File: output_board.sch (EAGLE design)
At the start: 27 parts, among them IC1 LTV-846PDIP16, IC2 LTV-846PDIP16, IC3 LTV-846PDIP16, IC4 LTV-846PDIP16

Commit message: Fixed bulk capacitor footprints; made +V for output channels independent on output board
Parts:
- removed IC3, IC4: LTV-846PDIP16, lichtenstein_onion:LTV-846PDIP16
- removed RN3, RN4: 1k, resistor-net:CTS742C083
- removed SV6, SV7, SV8, SV9: (no value), con-lstb:MA05-2
- SV2: value 1792928 -> 1792863; device lichtenstein_onion:1792928 -> lichtenstein_onion:1792863; MOUSER 651-1792928 -> (none)
- SV3: value 1792863 -> 1792928; device lichtenstein_onion:1792863 -> lichtenstein_onion:1792928; MOUSER (none) -> 651-1792928
- SV4, SV5: value 1792928 -> (none); device lichtenstein_onion:1792928 -> con-lstb:MA05-2; MOUSER 651-1792928 -> 517-30310-6002
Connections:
- removed net IN10: IC3.A3, SV5.3
- removed net IN11: IC3.A4, SV5.4
- removed net IN12: IC4.A1, SV5.5
- removed net IN13: IC4.A2, SV5.6
- removed net IN14: IC4.A3, SV5.7
- removed net IN15: IC4.A4, SV5.8
- removed net IN8: IC3.A1, SV5.1
- removed net IN9: IC3.A2, SV5.2
- removed net INPUT10: IC3.C3, SV9.8
- removed net INPUT11: IC3.C4, SV9.10
- removed net INPUT12: IC4.C1, SV9.3
- removed net INPUT13: IC4.C2, SV9.5
- removed net INPUT14: IC4.C3, SV9.7
- removed net INPUT15: IC4.C4, SV9.9
- removed net INPUT8: IC3.C1, SV9.4
- removed net INPUT9: IC3.C2, SV9.6
- removed net OUT10: RN3.3, SV2.3
- removed net OUT11: RN3.4, SV2.4
- removed net OUT12: RN4.1, SV2.5
- removed net OUT13: RN4.2, SV2.6
- removed net OUT14: RN4.3, SV2.7
- removed net OUT15: RN4.4, SV2.8
- removed net OUT8: RN3.1, SV2.1
- removed net OUT9: RN3.2, SV2.2
- removed net OUTPUT10: RN3.6, SV8.6
- removed net OUTPUT11: RN3.5, SV8.4
- removed net OUTPUT12: RN4.8, SV8.9
- removed net OUTPUT13: RN4.7, SV8.7
- removed net OUTPUT14: RN4.6, SV8.5
- removed net OUTPUT15: RN4.5, SV8.3
- removed net OUTPUT8: RN3.8, SV8.10
- removed net OUTPUT9: RN3.7, SV8.8
- net +5V: now also SV4.2, SV5.2; no longer SV6.2, SV7.2, SV8.2, SV9.2
- net GND: now also SV2.1, SV4.1, SV5.1; no longer IC3.E1, IC3.E2, IC3.E3, IC3.E4, IC3.K1, IC3.K2, IC3.K3, IC3.K4, IC4.E1, IC4.E2, IC4.E3, IC4.E4, IC4.K1, IC4.K2, IC4.K3, IC4.K4, SV3.1, SV6.1, SV7.1, SV8.1, SV9.1
- net IN0: now also SV3.1; no longer SV4.1
- net IN1: now also SV3.2; no longer SV4.2
- net IN2: now also SV3.3; no longer SV4.3
- net IN3: now also SV3.4; no longer SV4.4
- net IN4: now also SV3.5; no longer SV4.5
- net IN5: now also SV3.6; no longer SV4.6
- net IN6: now also SV3.7; no longer SV4.7
- net IN7: now also SV3.8; no longer SV4.8
- net INPUT0: now also SV5.4; no longer SV7.4
- net INPUT1: now also SV5.6; no longer SV7.6
- net INPUT2: now also SV5.8; no longer SV7.8
- net INPUT3: now also SV5.10; no longer SV7.10
- net INPUT4: now also SV5.3; no longer SV7.3
- net INPUT5: now also SV5.5; no longer SV7.5
- net INPUT6: now also SV5.7; no longer SV7.7
- net INPUT7: now also SV5.9; no longer SV7.9
- net OUTPUT0: now also SV4.10; no longer SV6.10
- net OUTPUT1: now also SV4.8; no longer SV6.8
- net OUTPUT2: now also SV4.6; no longer SV6.6
- net OUTPUT3: now also SV4.4; no longer SV6.4
- net OUTPUT4: now also SV4.9; no longer SV6.9
- net OUTPUT5: now also SV4.7; no longer SV6.7
- net OUTPUT6: now also SV4.5; no longer SV6.5
- net OUTPUT7: now also SV4.3; no longer SV6.3
- net V+: now also SV2.2; no longer SV3.2

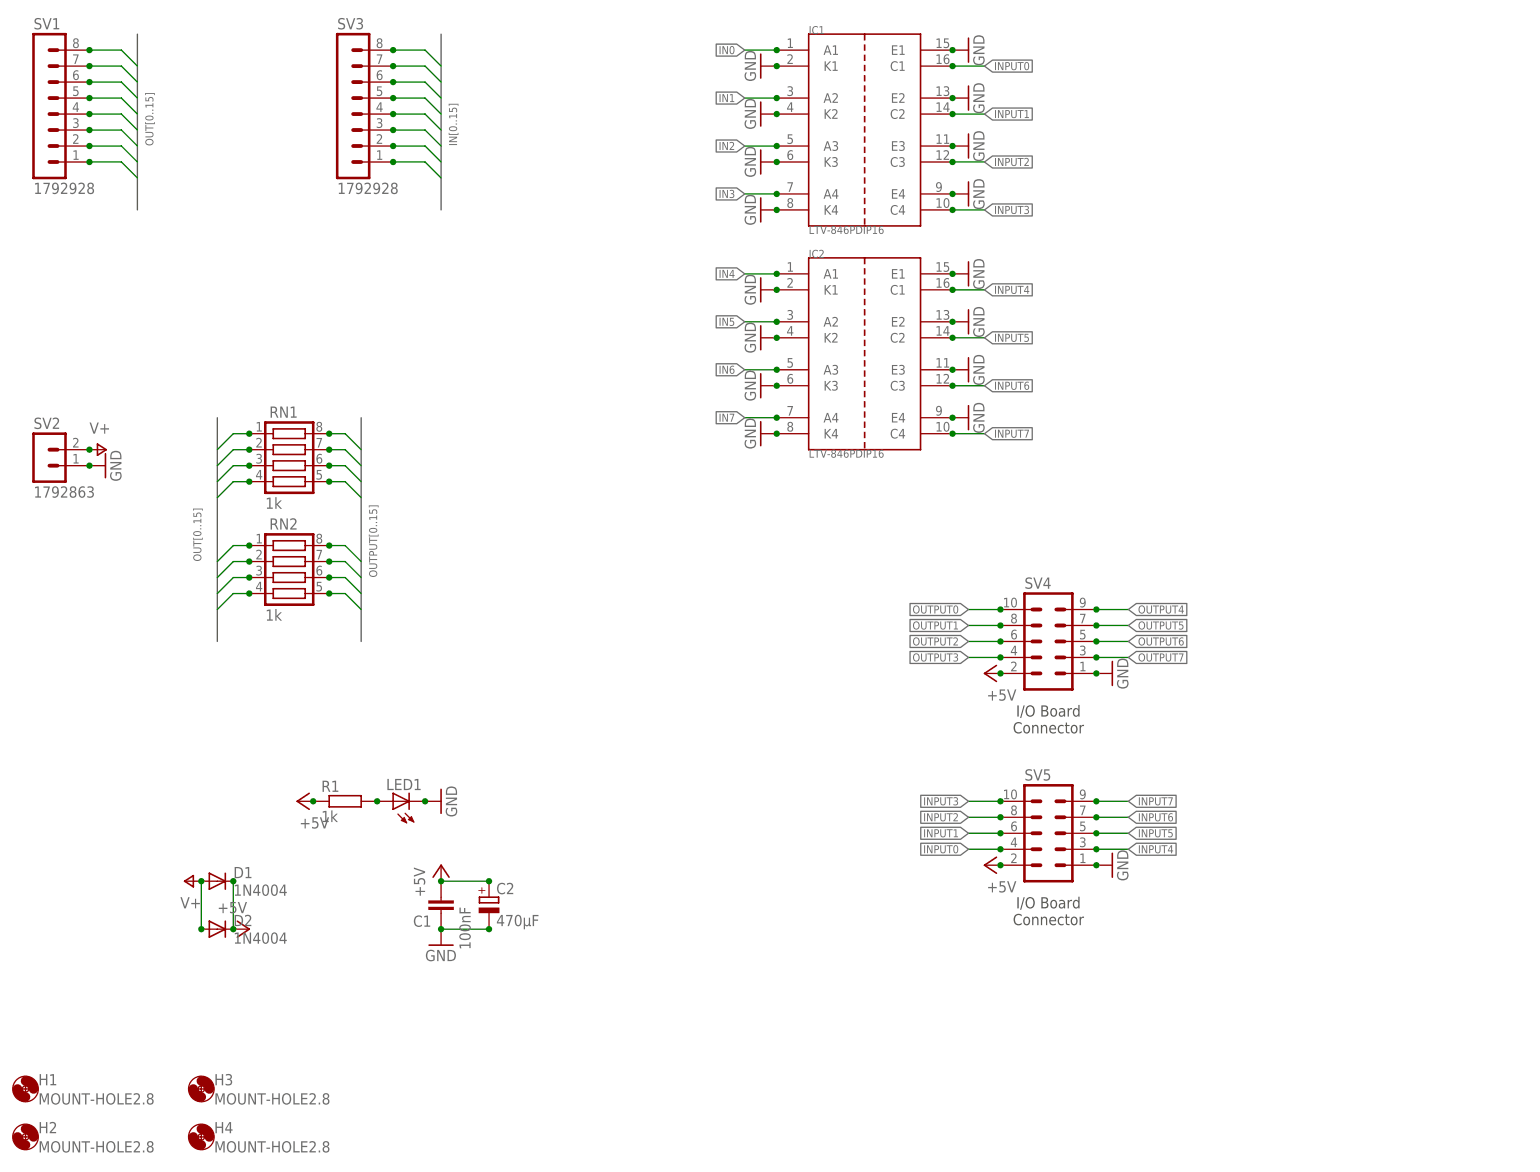
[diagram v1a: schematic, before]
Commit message: Cleaned up output board; added pull-ups to inputs on Lichtenstein board; moved some decoupling caps on FPGA output board
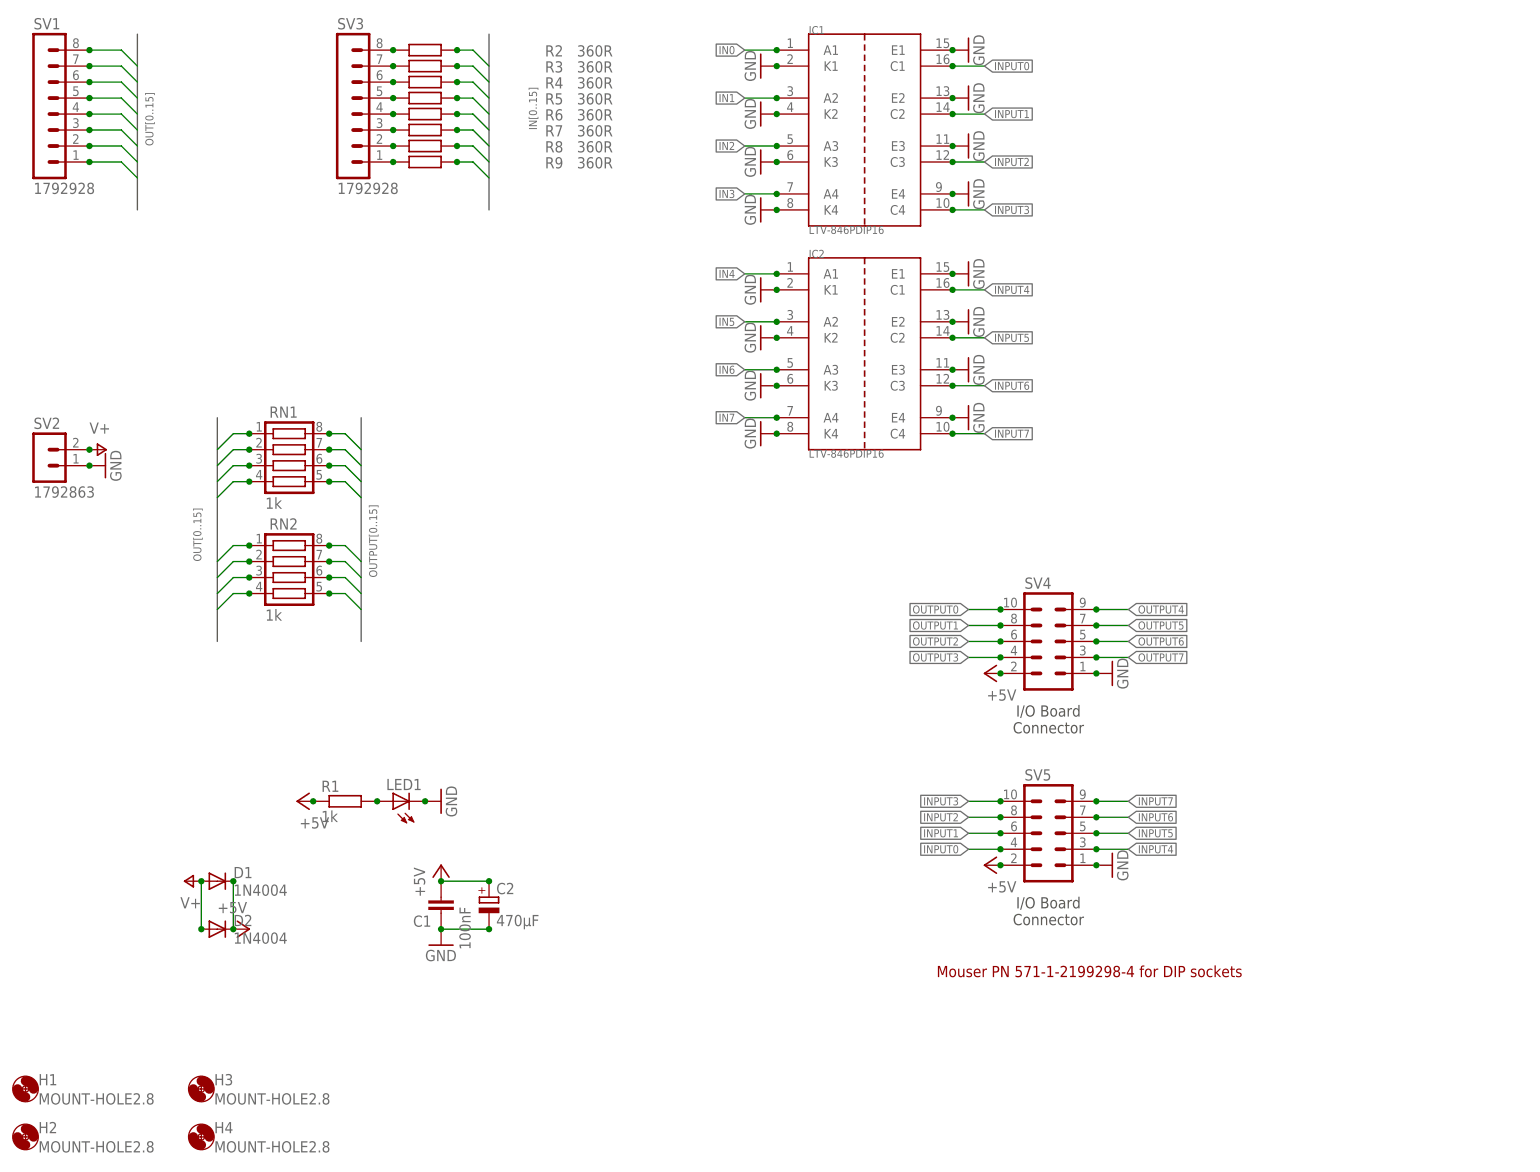
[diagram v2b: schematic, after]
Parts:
- added R2, R3, R4, R5, R6, R7, R8, R9: 360R, rcl:R-EU_M0805
- IC1, IC2: MOUSER (none) -> 859-LTV-846
- LED1: MOUSER 604-APTR3216SGC -> 604-APTR3216YC
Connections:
- new net N$2: R2.1, SV3.8
- new net N$3: R3.1, SV3.7
- new net N$4: R4.1, SV3.6
- new net N$5: R5.1, SV3.5
- new net N$6: R6.1, SV3.4
- new net N$7: R7.1, SV3.3
- new net N$8: R8.1, SV3.2
- new net N$9: R9.1, SV3.1
- net IN0: now also R9.2; no longer SV3.1
- net IN1: now also R8.2; no longer SV3.2
- net IN2: now also R7.2; no longer SV3.3
- net IN3: now also R6.2; no longer SV3.4
- net IN4: now also R5.2; no longer SV3.5
- net IN5: now also R4.2; no longer SV3.6
- net IN6: now also R3.2; no longer SV3.7
- net IN7: now also R2.2; no longer SV3.8
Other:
- note added: "Mouser PN 571-1-2199298-4 for DIP sockets"

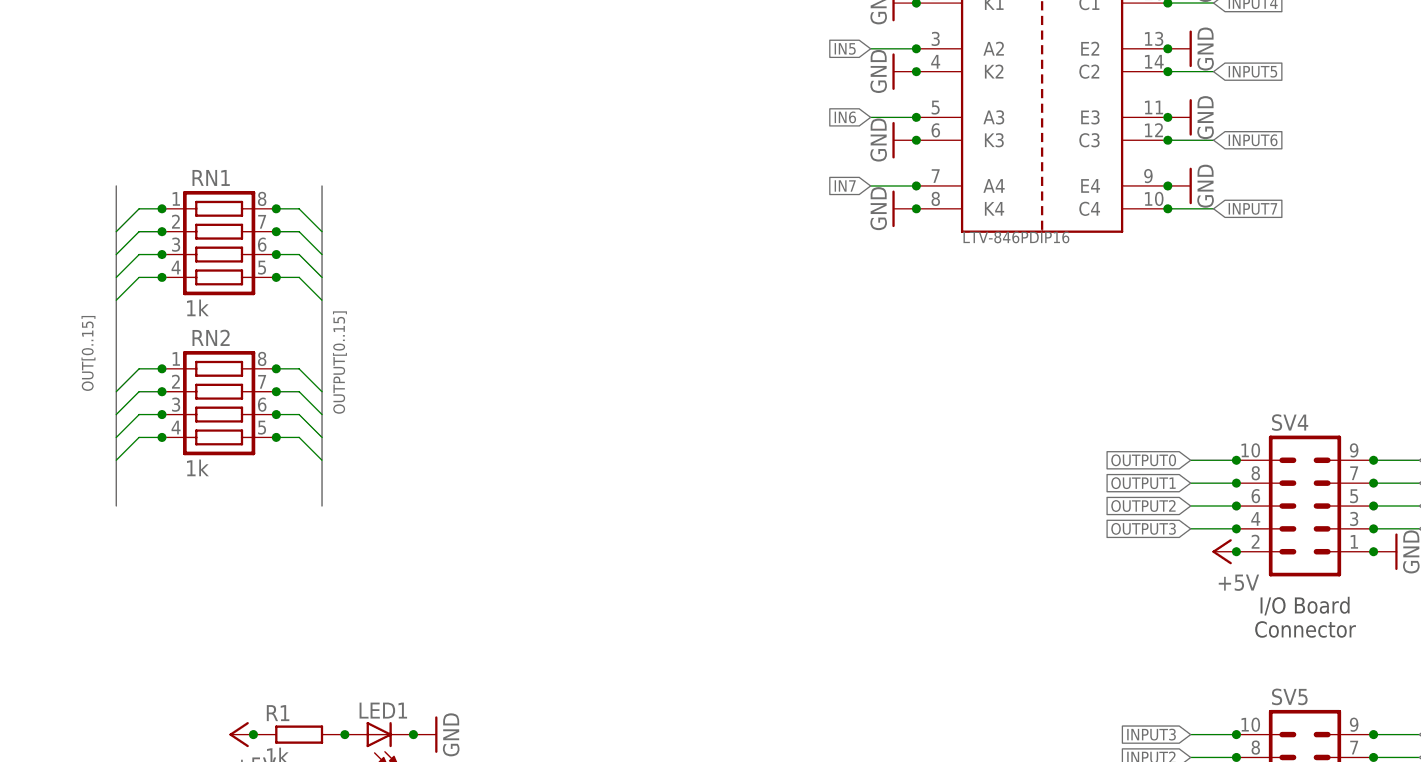
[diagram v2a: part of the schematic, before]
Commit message: Tweaked footprints for wire terminals; fixed up some mechanical issues on output board (incl. removing resistor networks)
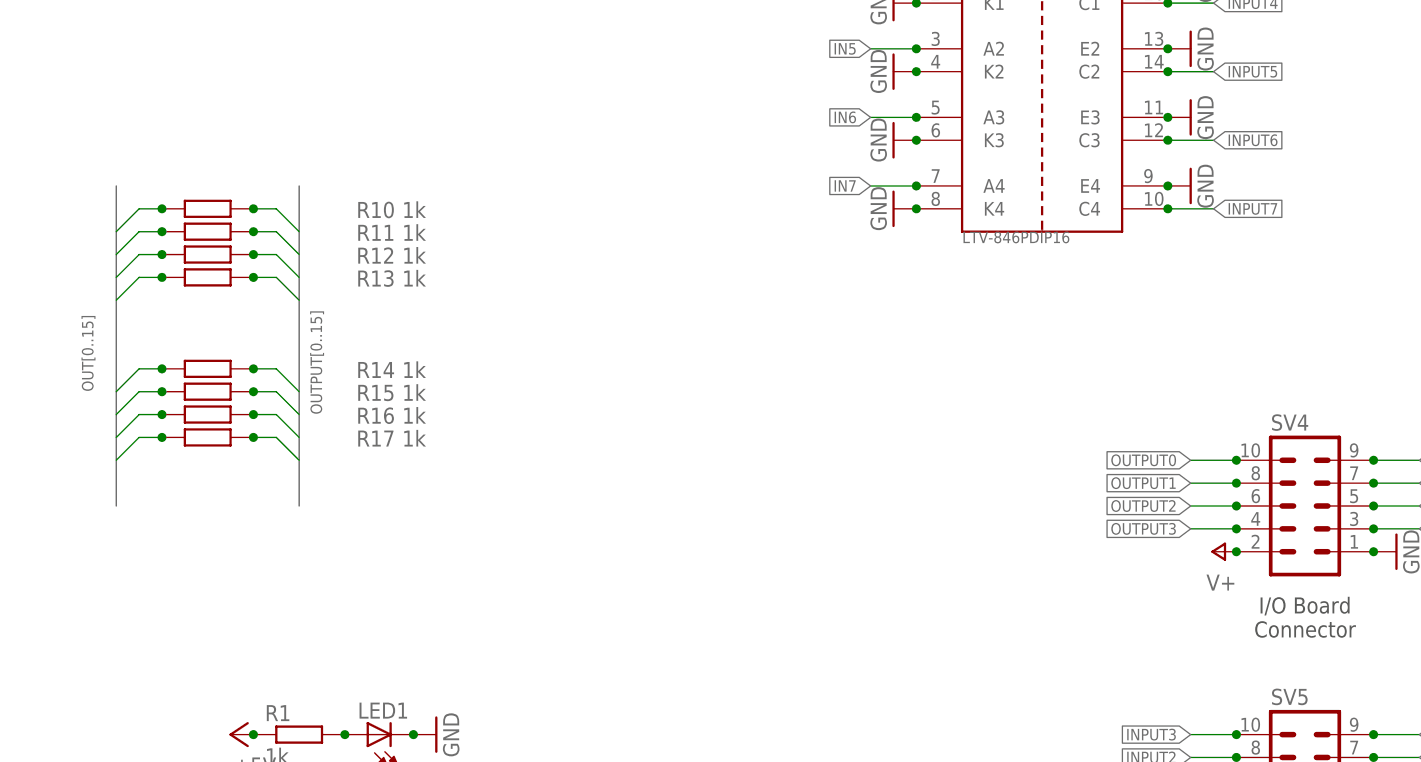
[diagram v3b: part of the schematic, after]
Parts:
- removed RN1, RN2: 1k, resistor-net:CTS742C083
- added R10, R11, R12, R13, R14, R15, R16, R17: 1k, rcl:R-EU_M0805
- C2: device rcl:CPOL-EUE5-13 -> rcl:CPOL-EUE5-10.5
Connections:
- net +5V: no longer SV4.2
- net OUT0: now also R10.1; no longer RN1.1
- net OUT1: now also R11.1; no longer RN1.2
- net OUT2: now also R12.1; no longer RN1.3
- net OUT3: now also R13.1; no longer RN1.4
- net OUT4: now also R14.1; no longer RN2.1
- net OUT5: now also R15.1; no longer RN2.2
- net OUT6: now also R16.1; no longer RN2.3
- net OUT7: now also R17.1; no longer RN2.4
- net OUTPUT0: now also R10.2; no longer RN1.8
- net OUTPUT1: now also R11.2; no longer RN1.7
- net OUTPUT2: now also R12.2; no longer RN1.6
- net OUTPUT3: now also R13.2; no longer RN1.5
- net OUTPUT4: now also R14.2; no longer RN2.8
- net OUTPUT5: now also R15.2; no longer RN2.7
- net OUTPUT6: now also R16.2; no longer RN2.6
- net OUTPUT7: now also R17.2; no longer RN2.5
- net V+: now also SV4.2

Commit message: Minor revisions to output board
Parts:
- R1: value 1k -> 360R; MOUSER 652-CR0805JW-102ELF -> 652-CR0805JW-361ELF
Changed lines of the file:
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@@
 <part name="P+3" library="supply1" library_urn="urn:adsk.eagle:library:371" deviceset="+5V" device=""/>
 <part name="P+2" library="supply1" library_urn="urn:adsk.eagle:library:371" deviceset="V+" device=""/>
-<part name="R1" library="rcl" library_urn="urn:adsk.eagle:library:334" deviceset="R-EU_" device="M0805" package3d_urn="urn:adsk.eagle:package:23556/1" value="1k">
-<attribute name="MOUSER" value="652-CR0805JW-102ELF"/>
+<part name="R1" library="rcl" library_urn="urn:adsk.eagle:library:334" deviceset="R-EU_" device="M0805" package3d_urn="urn:adsk.eagle:package:23556/1" value="360R">
+<attribute name="MOUSER" value="652-CR0805JW-361ELF"/>
 </part>
 <part name="LED1" library="led" library_urn="urn:adsk.eagle:library:259" deviceset="LED" device="CHIPLED_1206" package3d_urn="urn:adsk.eagle:package:15823/2">
